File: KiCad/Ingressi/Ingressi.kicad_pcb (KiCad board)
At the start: 2 copper layers, 100 x 65 mm, 6 parts, among them J1 SpeakON_NL4, J2 SpeakON_NL4, J3 Phoenix ZFKDSA, J4 JST_S4P-VH

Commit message: figerprint
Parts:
- added G***: LOGO, Ingressi:Fingerprint, B.Cu at (35.6, 57.4)
- added G***: LOGO, Ingressi:Fingerprint_SolderMask, B.Cu at (35.6, 57.4)

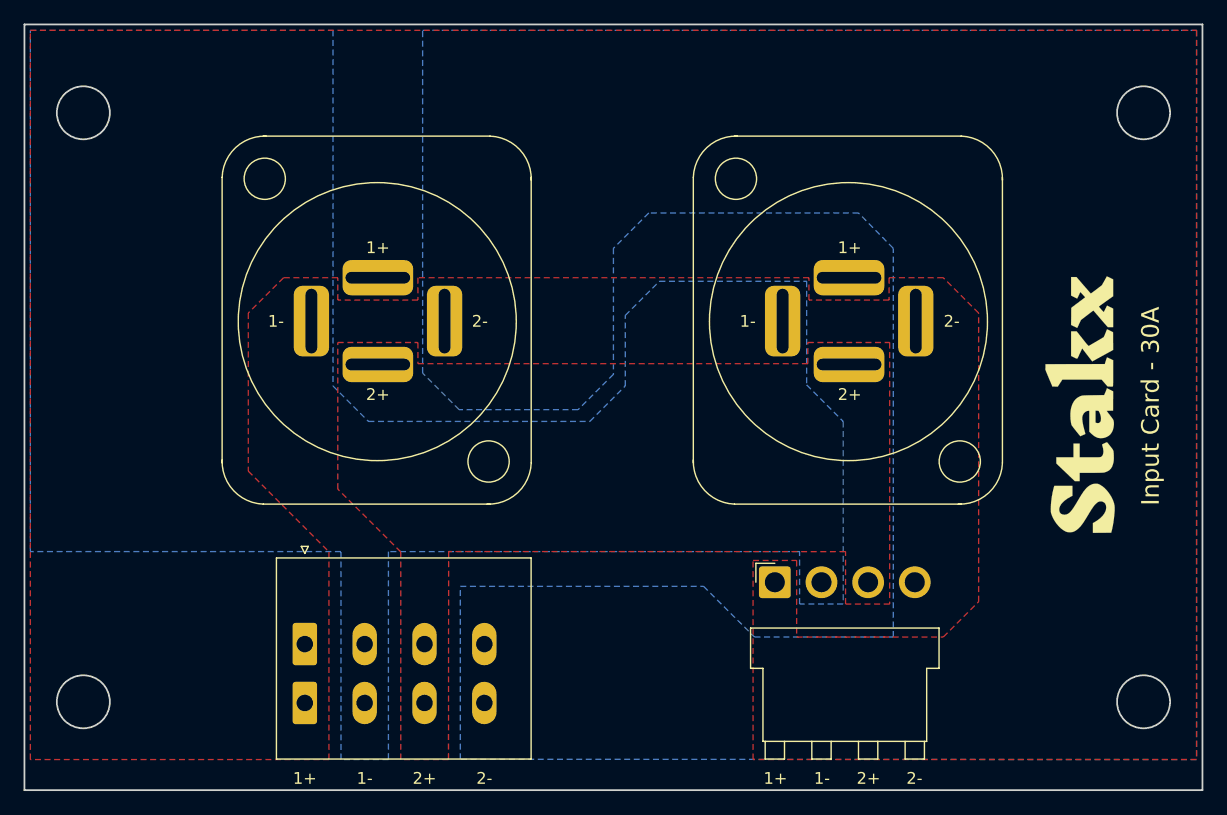
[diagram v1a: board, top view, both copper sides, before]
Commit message: added faston connector
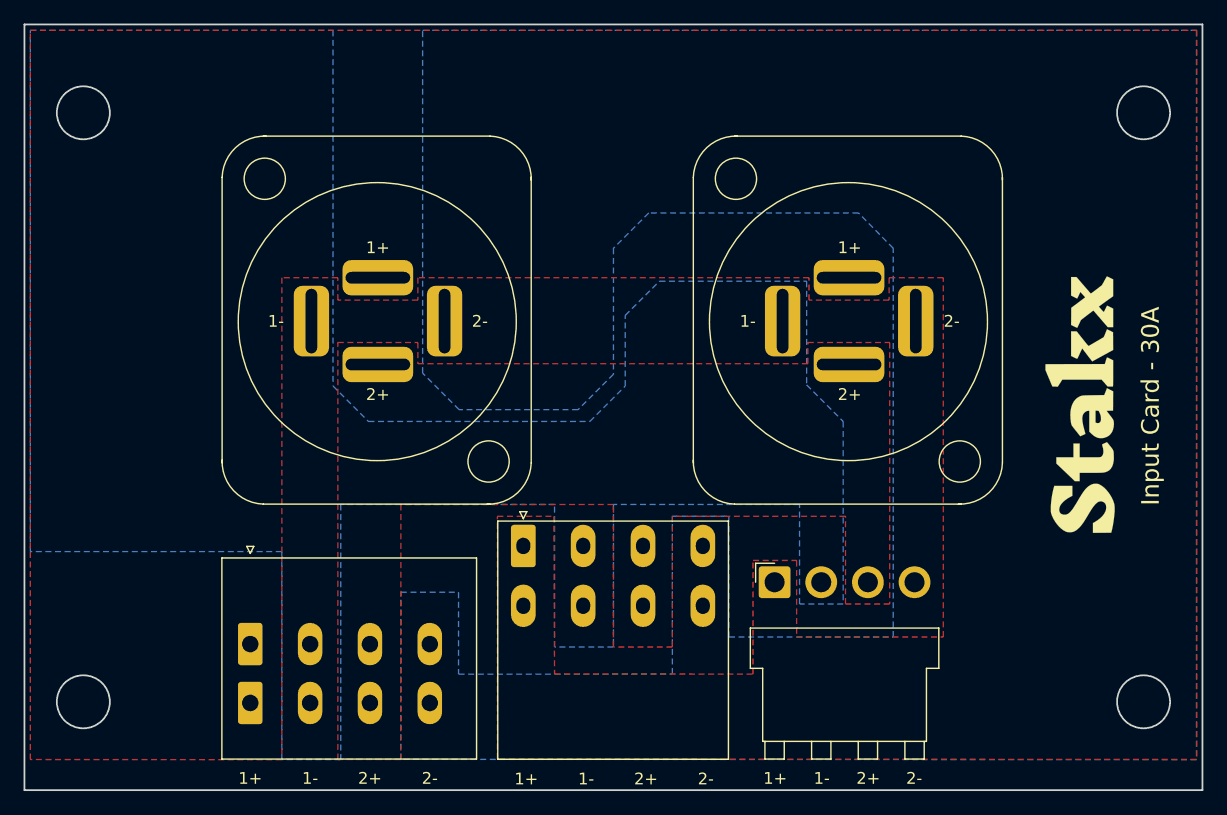
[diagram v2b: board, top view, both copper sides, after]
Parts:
- removed the G*** at (35.6, 57.4) (x2)
- added J5: Faston, Ingressi:Faston_01x04_P5.08mm_D5.08mm, F.Cu at (67.3, 69.3)
- J3: value Phoenix ZFKDSA -> Phoenix
- J4: value JST_S4P-VH -> JST
- moved J3 4.63 mm to (44.2, 82.6)
